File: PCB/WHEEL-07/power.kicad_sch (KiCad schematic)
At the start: 3 parts, among them IC2 LDO40LPU50RY

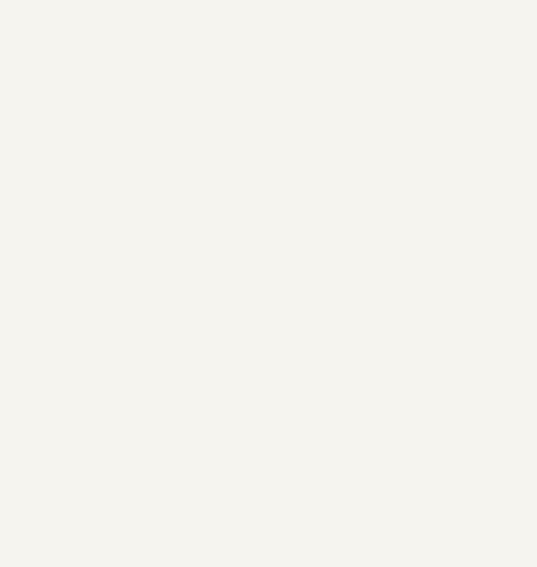
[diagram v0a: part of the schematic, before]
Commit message: Configured library loader for this project
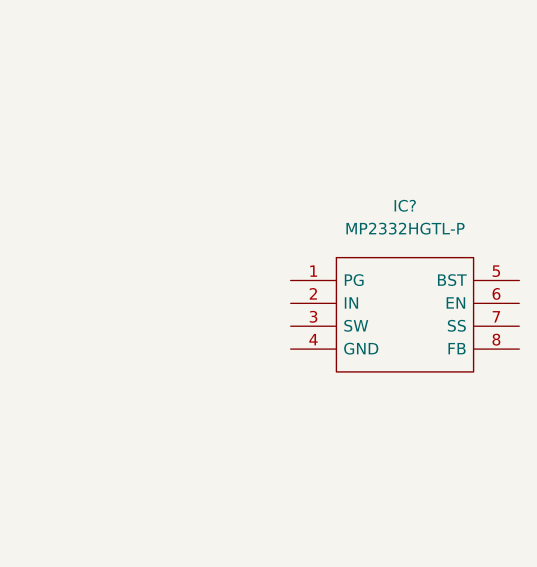
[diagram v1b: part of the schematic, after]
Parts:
- added IC?: MP2332HGTL-P, SOTFL50P160X60-8N, symbol WHEEL_07_LIBRARY_LOADER:MP2332HGTL-P
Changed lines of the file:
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@@
     (pin "1")
+  )
+  (symbol (lib_id "WHEEL_07_LIBRARY_LOADER:MP2332HGTL-P") (at 172.085 51.435 0) (unit 1)
+    (in_bom yes) (on_board yes) (fields_autoplaced)
+    (property "Reference" "IC?" (id 0) (at 184.785 43.18 0))
+    (property "Value" "MP2332HGTL-P" (id 1) (at 184.785 45.72 0))
+    (property "Footprint" "SOTFL50P160X60-8N" (id 2) (at 193.675 48.895 0)
+      (effects (font (size 1.27 1.27)) (justify left) hide)
+    )
+    (property "Datasheet" "https://eu.mouser.com/datasheet/2/277/MP2332H-1624281.pdf" (id 3) (at 193.675 51.435 0)
+      (effects (font (size 1.27 1.27)) (justify left) hide)
+    )
+    (property "Description" "Switching Voltage Regulators High-Efficiency, 2A, 18V, 1200kHz, Synchronous, Step-Down Converter" (id 4) (at 193.675 53.975 0)
+      (effects (font (size 1.27 1.27)) (justify left) hide)
+    )
+    (property "Height" "0.6" (id 5) (at 193.675 56.515 0)
+      (effects (font (size 1.27 1.27)) (justify left) hide)
+    )
+    (property "Manufacturer_Name" "Monolithic Power Systems (MPS)" (id 6) (at 193.675 59.055 0)
+      (effects (font (size 1.27 1.27)) (justify left) hide)
+    )
+    (property "Manufacturer_Part_Number" "MP2332HGTL-P" (id 7) (at 193.675 61.595 0)
+      (effects (font (size 1.27 1.27)) (justify left) hide)
+    )
+    (property "Mouser Part Number" "946-MP2332HGTL-P" (id 8) (at 193.675 64.135 0)
+      (effects (font (size 1.27 1.27)) (justify left) hide)
+    )
+    (property "Mouser Price/Stock" "https://www.mouser.co.uk/ProductDetail/Monolithic-Power-Systems-MPS/MP2332HGTL-P?qs=%252B6g0mu59x7LDoxfvqJ695A%3D%3D" (id 9) (at 193.675 66.675 0)
+      (effects (font (size 1.27 1.27)) (justify left) hide)
+    )
+    (property "Arrow Part Number" "" (id 10) (at 193.675 69.215 0)
+      (effects (font (size 1.27 1.27)) (justify left) hide)
+    )
+    (property "Arrow Price/Stock" "" (id 11) (at 193.675 71.755 0)
+      (effects (font (size 1.27 1.27)) (justify left) hide)
+    )
+    (pin "1")
+    (pin "2")
+    (pin "3")
+    (pin "4")
+    (pin "5")
+    (pin "6")
+    (pin "7")
+    (pin "8")
   )
   (symbol (lib_id "power:PWR_FLAG") (at 59.055 62.865 270) (unit 1)

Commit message: Finished power section
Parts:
- added C?: 0.1uF, symbol Device:C_Small
- added C? (x3): 22uF, symbol Device:C_Small
- added C?: 10pF, symbol Device:C_Small
- added C?: 1nF, symbol Device:C_Small
- added C?: 6.8nF, symbol Device:C_Small
- added C?: 1uF, symbol Device:C_Small
- added L?: 2.2uH, symbol Device:L_Small
- added R?: 20k, symbol Device:R_Small
- added R?: 20, symbol Device:R_Small
- added R?: 40.2k, symbol Device:R_Small
- added R?: 200k, symbol Device:R_Small
- added R?: 13k, symbol Device:R_Small
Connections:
- net +12V: now also IC?.2 (IN), C?.2, C?.2, R?.2
- net GND: now also IC?.4 (GND), C?.1, C?.1, C?.1, C?.1, C?.1, C?.1, R?.2
- net PG3V3: now reaches IC?.1 (PG)
- net PG3V3: now also C?.2
- net at IC?.3 (SW): now also C?.2, L?.1
- net at IC?.5 (BST): now also R?.1
- net at IC?.6 (EN): now also R?.1
- net at IC?.7 (SS): now also C?.2
- net at IC?.8 (FB): now also R?.2
- new net: C?.1, R?.1, R?.1, R?.2
- new net: C?.1, R?.2
- new net +3.3V: C?.2, C?.2, C?.2, L?.2, R?.1
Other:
- note added: "3.3V BUCK SECTION"
- note added: "POWER SECTION"
- moved on the sheet: IC?

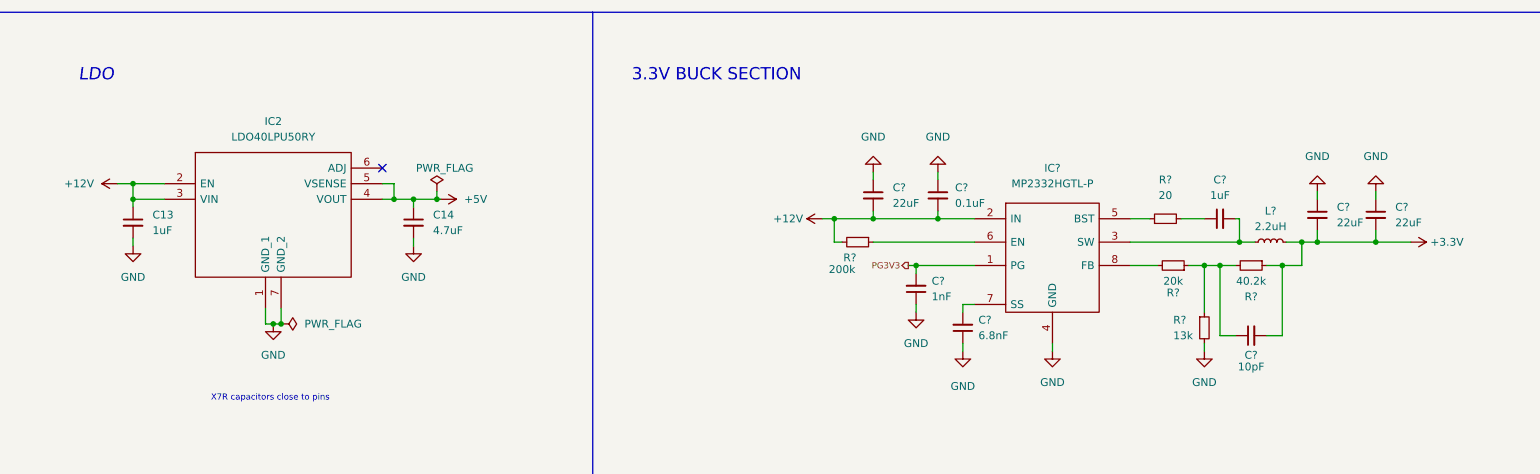
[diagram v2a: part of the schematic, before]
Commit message: Modified layout
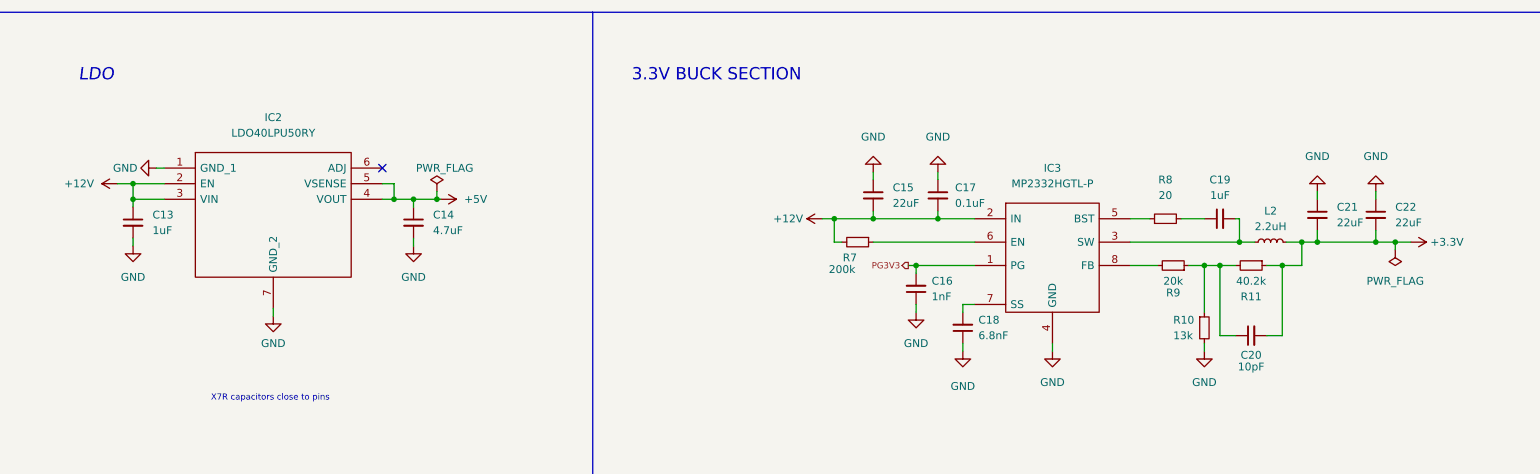
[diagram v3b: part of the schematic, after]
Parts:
- removed IC2: LDO40LPU50RY, BSPD_07:SON95P300X300X90-7N-D, symbol BSPD-07:LDO40LPU50RY
- added IC2: LDO40LPU50RY, SON95P300X300X90-7N-D, symbol WHEEL_07:LDO40LPU50RY
- IC3: renamed from IC?; footprint SOTFL50P160X60-8N -> WHEEL_07_LIBRARY_LOADER:SOTFL50P160X60-8N
- R10, R11, R7, R8, R9: renamed from R?; footprint (none) -> Resistor_SMD:R_0402_1005Metric
- gave numbers to parts that had none: 9
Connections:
- net +12V: now also IC2.2 (EN), IC2.3 (VIN)
- net +5V: now also IC2.4 (VOUT), IC2.5 (VSENSE)
- net GND: now also IC2.1 (GND_1), IC2.7 (GND_2)

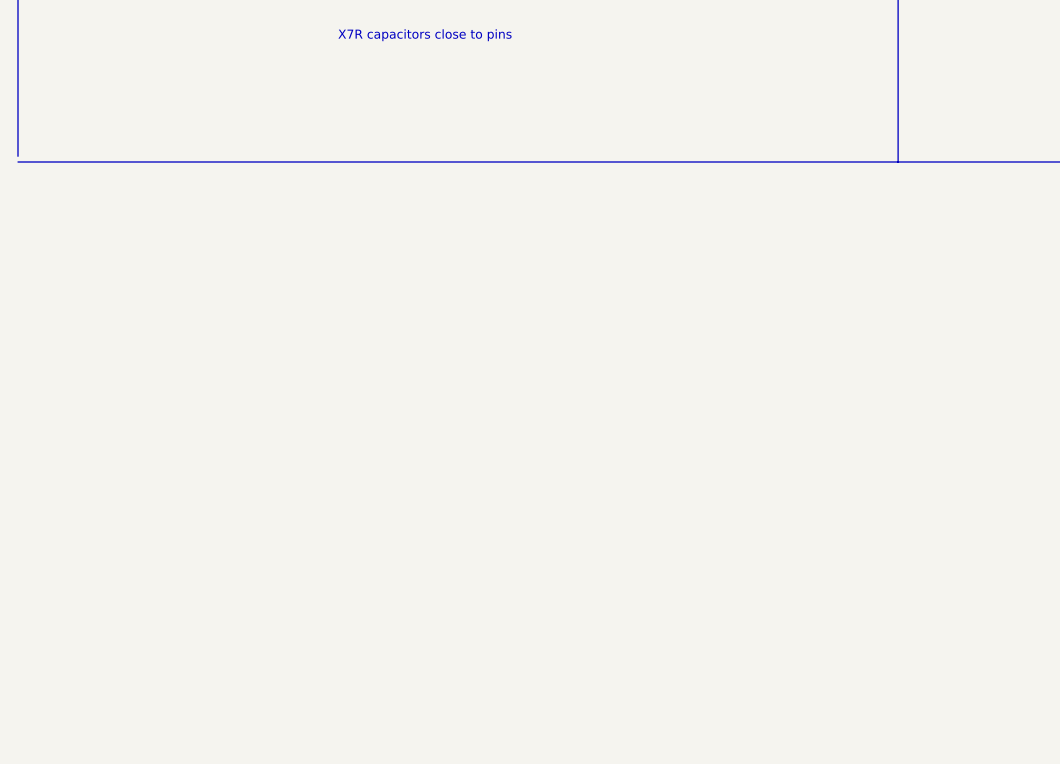
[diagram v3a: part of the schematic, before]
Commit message: Modified schematics & assigned all footprints
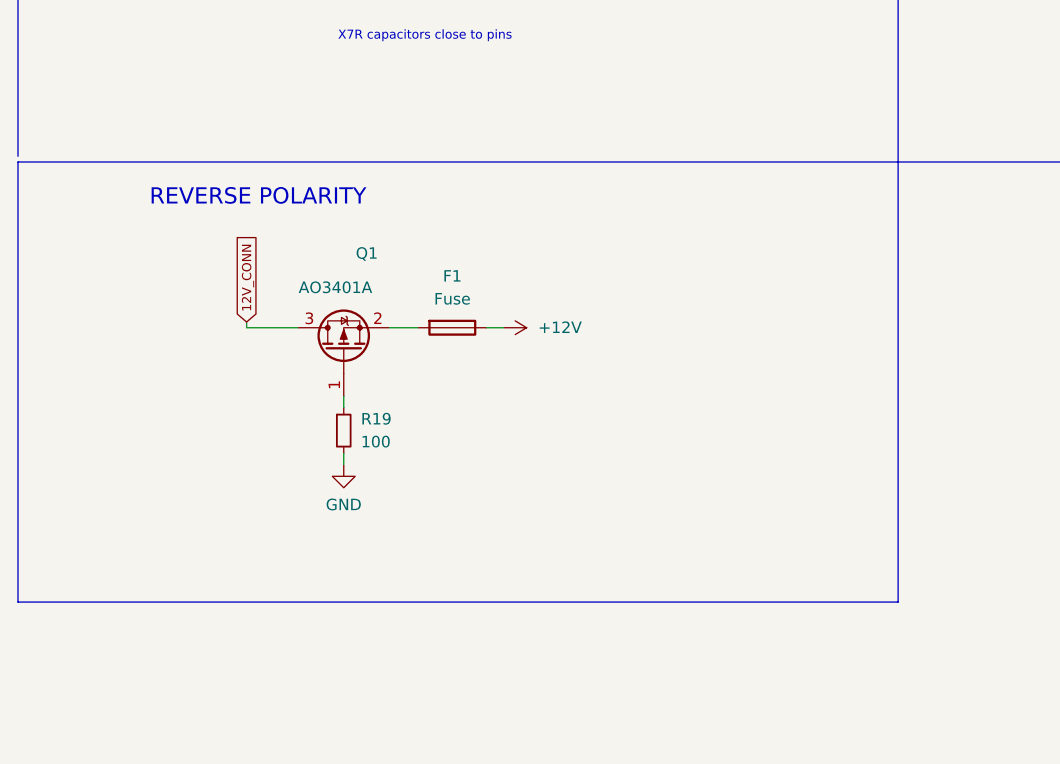
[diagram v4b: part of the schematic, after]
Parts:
- added F1: Fuse, Fuse:Fuse_0805_2012Metric, symbol Device:Fuse
- added Q1: AO3401A, Package_TO_SOT_SMD:SOT-23, symbol Transistor_FET:AO3401A
- added R19: 100, Resistor_SMD:R_0402_1005Metric, symbol Device:R_Small
- C14: footprint Capacitor_SMD:C_0805_2012Metric -> Capacitor_SMD:C_0201_0603Metric
- C15, C21, C22: footprint (none) -> Capacitor_SMD:C_0402_1005Metric
- IC2: footprint SON95P300X300X90-7N-D -> WHEEL-07:SON95P300X300X90-7N-D
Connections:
- net +12V: now also F1.1
- net GND: now also R19.2
- new net: Q1.1 (G), R19.1
- new net: F1.2, Q1.2 (S)
- new net 12V_CONN: Q1.3 (D)
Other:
- note added: "REVERSE POLARITY"
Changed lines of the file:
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@@
+    (stroke (width 0) (type default) (color 0 0 0 0))
+  )
+  (wire (pts (xy 48.26 114.935) (xy 48.26 116.205))
     (stroke (width 0) (type default) (color 0 0 0 0))
   )
@@
     (stroke (width 0) (type default) (color 0 0 0 0))
   )
+  (wire (pts (xy 48.26 121.285) (xy 48.26 122.555))
+    (stroke (width 0) (type default) (color 0 0 0 0))
+  )
   (wire (pts (xy 57.785 60.325) (xy 57.785 61.595))
     (stroke (width 0) (type default) (color 0 0 0 0))
@@
     (stroke (width 0) (type default) (color 0 0 0 0))
   )
+  (wire (pts (xy 37.465 107.315) (xy 43.18 107.315))
+    (stroke (width 0) (type default) (color 0 0 0 0))
+  )
+  (wire (pts (xy 64.135 107.315) (xy 66.04 107.315))
+    (stroke (width 0) (type default) (color 0 0 0 0))
+  )
   (wire (pts (xy 77.47 40.005) (xy 77.47 42.545))
     (stroke (width 0) (type default) (color 0 0 0 0))
@@
     (stroke (width 0) (type default) (color 0 0 0 0))
   )
+  (polyline (pts (xy 12.065 137.795) (xy 109.855 137.795))
+    (stroke (width 0) (type default) (color 0 0 0 0))
+  )
   (polyline (pts (xy 109.855 88.9) (xy 285.115 88.9))
     (stroke (width 0) (type default) (color 0 0 0 0))
@@
     (stroke (width 0) (type default) (color 0 0 0 0))
   )
+  (polyline (pts (xy 109.855 137.795) (xy 109.855 88.9))
+    (stroke (width 0) (type default) (color 0 0 0 0))
+  )
   (wire (pts (xy 215.265 49.53) (xy 215.265 45.72))
     (stroke (width 0) (type default) (color 0 0 0 0))
@@
     (stroke (width 0) (type default) (color 0 0 0 0))
   )
+  (polyline (pts (xy 12.065 88.9) (xy 12.065 137.795))
+    (stroke (width 0) (type default) (color 0 0 0 0))
+  )
   (wire (pts (xy 205.74 45.72) (xy 209.55 45.72))
     (stroke (width 0) (type default) (color 0 0 0 0))
@@
     (stroke (width 0) (type default) (color 0 0 0 0))
   )
+  (wire (pts (xy 53.34 107.315) (xy 56.515 107.315))
+    (stroke (width 0) (type default) (color 0 0 0 0))
+  )
   (wire (pts (xy 237.49 47.625) (xy 237.49 49.53))
     (stroke (width 0) (type default) (color 0 0 0 0))
   )
   (wire (pts (xy 219.71 64.77) (xy 222.25 64.77))
+    (stroke (width 0) (type default) (color 0 0 0 0))
+  )
+  (wire (pts (xy 37.465 106.68) (xy 37.465 107.315))
     (stroke (width 0) (type default) (color 0 0 0 0))
   )
@@
   (text "LDO" (at 26.035 23.495 0)
     (effects (font (size 2 2) italic) (justify left bottom))
+  )
+  (text "REVERSE POLARITY" (at 26.67 93.98 0)
+    (effects (font (size 1.8 1.8)) (justify left bottom))
+  )
+  (global_label "12V_CONN" (shape input) (at 37.465 106.68 90) (fields_autoplaced)
+    (effects (font (size 1.016 1.016)) (justify left))
+    (property "Intersheet References" "${INTERSHEET_REFS}" (id 0) (at 37.4015 96.9603 90)
+      (effects (font (size 1.016 1.016)) (justify left) hide)
+    )
   )
   (hierarchical_label "PG3V3" (shape output) (at 161.29 53.34 180)
@@
     (pin "2")
   )
+  (symbol (lib_id "Device:R_Small") (at 48.26 118.745 0) (unit 1)
+    (in_bom yes) (on_board yes) (fields_autoplaced)
+    (property "Reference" "R19" (id 0) (at 50.165 117.4749 0)
+      (effects (font (size 1.27 1.27)) (justify left))
+    )
+    (property "Value" "100" (id 1) (at 50.165 120.0149 0)
+      (effects (font (size 1.27 1.27)) (justify left))
+    )
+    (property "Footprint" "Resistor_SMD:R_0402_1005Metric" (id 2) (at 48.26 118.745 0)
+      (effects (font (size 1.27 1.27)) hide)
+    )
+    (property "Datasheet" "~" (id 3) (at 48.26 118.745 0)
+      (effects (font (size 1.27 1.27)) hide)
+    )
+    (pin "1")
+    (pin "2")
+  )
   (symbol (lib_id "WHEEL_07:LDO40LPU50RY") (at 40.005 37.465 0) (unit 1)
     (in_bom yes) (on_board yes) (fields_autoplaced)
     (property "Reference" "IC2" (id 0) (at 57.785 29.21 0))
     (property "Value" "LDO40LPU50RY" (id 1) (at 57.785 31.75 0))
-    (property "Footprint" "SON95P300X300X90-7N-D" (id 2) (at 71.755 34.925 0)
+    (property "Footprint" "WHEEL-07:SON95P300X300X90-7N-D" (id 2) (at 71.755 34.925 0)
       (effects (font (size 1.27 1.27)) (justify left) hide)
     )
@@
     (pin "1")
   )
+  (symbol (lib_id "Transistor_FET:AO3401A") (at 48.26 109.855 90) (unit 1)
+    (in_bom yes) (on_board yes)
+    (property "Reference" "Q1" (id 0) (at 52.07 99.0601 90)
+      (effects (font (size 1.27 1.27)) (justify left))
+    )
+    (property "Value" "AO3401A" (id 1) (at 51.435 102.87 90)
+      (effects (font (size 1.27 1.27)) (justify left))
+    )
+    (property "Footprint" "Package_TO_SOT_SMD:SOT-23" (id 2) (at 50.165 104.775 0)
+      (effects (font (size 1.27 1.27) italic) (justify left) hide)
+    )
+    (property "Datasheet" "http://www.aosmd.com/pdfs/datasheet/AO3401A.pdf" (id 3) (at 48.26 109.855 0)
+      (effects (font (size 1.27 1.27)) (justify left) hide)
+    )
+    (pin "1")
+    (pin "2")
+    (pin "3")
+  )
   (symbol (lib_id "Device:R_Small") (at 217.17 53.34 270) (unit 1)
     (in_bom yes) (on_board yes)
@@
       (effects (font (size 1.27 1.27)) (justify left))
     )
-    (property "Footprint" "" (id 2) (at 227.965 45.085 0)
+    (property "Footprint" "Capacitor_SMD:C_0402_1005Metric" (id 2) (at 227.965 45.085 0)
       (effects (font (size 1.27 1.27)) hide)
     )
@@
     )
     (pin "1")
+  )
+  (symbol (lib_id "Device:Fuse") (at 60.325 107.315 270) (unit 1)
+    (in_bom yes) (on_board yes) (fields_autoplaced)
+    (property "Reference" "F1" (id 0) (at 60.325 101.6 90))
+    (property "Value" "Fuse" (id 1) (at 60.325 104.14 90))
+    (property "Footprint" "Fuse:Fuse_0805_2012Metric" (id 2) (at 60.325 105.537 90)
+      (effects (font (size 1.27 1.27)) hide)
+    )
+    (property "Datasheet" "~" (id 3) (at 60.325 107.315 0)
+      (effects (font (size 1.27 1.27)) hide)
+    )
+    (pin "1")
+    (pin "2")
   )
   (symbol (lib_id "power:GND") (at 80.645 50.165 0) (unit 1)
@@
     )
     (property "Datasheet" "" (id 3) (at 80.645 50.165 0)
+      (effects (font (size 1.27 1.27)) hide)
+    )
+    (pin "1")
+  )
+  (symbol (lib_id "power:GND") (at 48.26 122.555 0) (unit 1)
+    (in_bom yes) (on_board yes) (fields_autoplaced)
+    (property "Reference" "#PWR0168" (id 0) (at 48.26 128.905 0)
+      (effects (font (size 1.27 1.27)) hide)
+    )
+    (property "Value" "GND" (id 1) (at 48.26 127 0))
+    (property "Footprint" "" (id 2) (at 48.26 122.555 0)
+      (effects (font (size 1.27 1.27)) hide)
+    )
+    (property "Datasheet" "" (id 3) (at 48.26 122.555 0)
       (effects (font (size 1.27 1.27)) hide)
     )
@@
     (pin "2")
   )
+  (symbol (lib_id "power:+12V") (at 66.04 107.315 270) (unit 1)
+    (in_bom yes) (on_board yes) (fields_autoplaced)
+    (property "Reference" "#PWR0167" (id 0) (at 62.23 107.315 0)
+      (effects (font (size 1.27 1.27)) hide)
+    )
+    (property "Value" "+12V" (id 1) (at 69.85 107.3149 90)
+      (effects (font (size 1.27 1.27)) (justify left))
+    )
+    (property "Footprint" "" (id 2) (at 66.04 107.315 0)
+      (effects (font (size 1.27 1.27)) hide)
+    )
+    (property "Datasheet" "" (id 3) (at 66.04 107.315 0)
+      (effects (font (size 1.27 1.27)) hide)
+    )
+    (pin "1")
+  )
   (symbol (lib_id "Device:C_Small") (at 237.49 45.085 0) (unit 1)
     (in_bom yes) (on_board yes) (fields_autoplaced)
@@
       (effects (font (size 1.27 1.27)) (justify left))
     )
-    (property "Footprint" "" (id 2) (at 237.49 45.085 0)
+    (property "Footprint" "Capacitor_SMD:C_0402_1005Metric" (id 2) (at 237.49 45.085 0)
       (effects (font (size 1.27 1.27)) hide)
     )
@@
       (effects (font (size 1.27 1.27)) (justify left))
     )
-    (property "Footprint" "Capacitor_SMD:C_0805_2012Metric" (id 2) (at 80.645 46.355 0)
+    (property "Footprint" "Capacitor_SMD:C_0201_0603Metric" (id 2) (at 80.645 46.355 0)
       (effects (font (size 1.27 1.27)) hide)
     )
@@
       (effects (font (size 1.27 1.27)) (justify left))
     )
-    (property "Footprint" "" (id 2) (at 155.575 41.91 0)
-      (effects (font (size 1.27 1.27)) hide)
-    )
+    (property "Footprint" "Capacitor_SMD:C_0402_1005Metric" (id 2) (at 155.575 41.91 0)
+      (effects (font (size 1.27 1.27)) hide)
+    )
